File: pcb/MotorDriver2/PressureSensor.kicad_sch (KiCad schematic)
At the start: 22 parts, among them J2 Conn_01x02, J3 Conn_01x02, J4 Conn_01x02, J5 Conn_01x02, U6 LM324DR

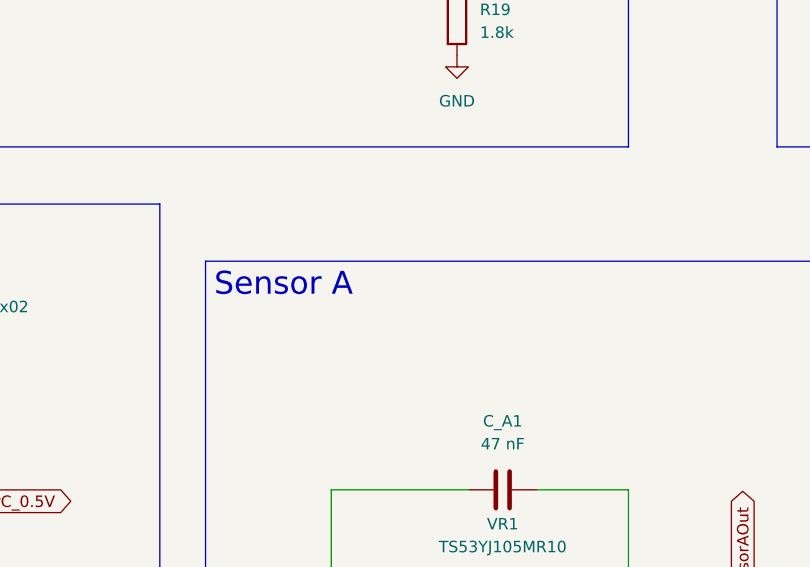
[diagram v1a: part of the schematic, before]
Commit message: Modified pwm pins
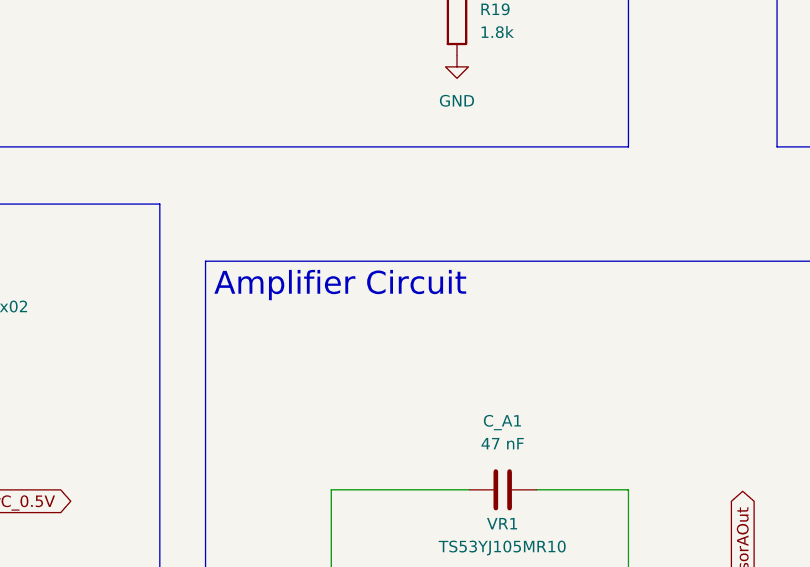
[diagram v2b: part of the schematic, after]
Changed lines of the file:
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@@
 	(generator_version "9.0")
 	(paper "A4")
-	(text_box "Sensor A\n"
+	(text_box "Amplifier Circuit"
 		(exclude_from_sim no)
 		(at 90.17 66.04 0)

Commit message: Laying out PCB
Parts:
- C_A1: LCSC (none) -> C77012
- R18, R19: LCSC (none) -> C25871
- U6: footprint footprintLib:D14 -> CapstoneFootprints:D14
- VR1, VR2, VR3, VR4: footprint footprintLib:TS53YJ105MR10 -> CapstoneFootprints:TS53YJ105MR10
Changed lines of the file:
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@@
 		(dnp no)
 		(fields_autoplaced yes)
-		(property "Reference" "#PWR065"
+		(property "Reference" "#PWR025"
 			(at 60.96 111.76 0)
 			(effects
@@
 			(project "MotorDriver1"
 				(path "/6e0510ec-6dbc-4bc1-a315-3680b1127a92/84d965bc-7f0b-4bc5-931c-8ce848efd12b"
-					(reference "#PWR065")
+					(reference "#PWR025")
 					(unit 1)
 				)
@@
 		(dnp no)
 		(fields_autoplaced yes)
-		(property "Reference" "#PWR042"
+		(property "Reference" "#PWR026"
 			(at 60.96 171.45 0)
 			(effects
@@
 			(project "MotorDriver1"
 				(path "/6e0510ec-6dbc-4bc1-a315-3680b1127a92/84d965bc-7f0b-4bc5-931c-8ce848efd12b"
-					(reference "#PWR042")
+					(reference "#PWR026")
 					(unit 1)
 				)
@@
 			)
 		)
+		(property "LCSC" "C25871"
+			(at 118.11 39.37 0)
+			(effects
+				(font
+					(size 1.27 1.27)
+				)
+				(hide yes)
+			)
+		)
 		(pin "2"
 		)
@@
 		(dnp no)
 		(fields_autoplaced yes)
-		(property "Reference" "#PWR062"
+		(property "Reference" "#PWR029"
 			(at 185.42 40.64 0)
 			(effects
@@
 			(project "MotorDriver1"
 				(path "/6e0510ec-6dbc-4bc1-a315-3680b1127a92/84d965bc-7f0b-4bc5-931c-8ce848efd12b"
-					(reference "#PWR062")
+					(reference "#PWR029")
 					(unit 1)
 				)
@@
 		(dnp no)
 		(fields_autoplaced yes)
-		(property "Reference" "#PWR064"
+		(property "Reference" "#PWR023"
 			(at 52.07 77.47 0)
 			(effects
@@
 			(project "MotorDriver1"
 				(path "/6e0510ec-6dbc-4bc1-a315-3680b1127a92/84d965bc-7f0b-4bc5-931c-8ce848efd12b"
-					(reference "#PWR064")
+					(reference "#PWR023")
 					(unit 1)
 				)
@@
 		(dnp no)
 		(fields_autoplaced yes)
-		(property "Reference" "#PWR041"
+		(property "Reference" "#PWR024"
 			(at 52.07 137.16 0)
 			(effects
@@
 			(project "MotorDriver1"
 				(path "/6e0510ec-6dbc-4bc1-a315-3680b1127a92/84d965bc-7f0b-4bc5-931c-8ce848efd12b"
-					(reference "#PWR041")
+					(reference "#PWR024")
 					(unit 1)
 				)
@@
 		(dnp no)
 		(fields_autoplaced yes)
-		(property "Reference" "#PWR043"
+		(property "Reference" "#PWR028"
 			(at 118.11 49.53 0)
 			(effects
@@
 			(project "MotorDriver1"
 				(path "/6e0510ec-6dbc-4bc1-a315-3680b1127a92/84d965bc-7f0b-4bc5-931c-8ce848efd12b"
-					(reference "#PWR043")
+					(reference "#PWR028")
 					(unit 1)
 				)
@@
 		(dnp no)
 		(fields_autoplaced yes)
-		(property "Reference" "#PWR040"
+		(property "Reference" "#PWR027"
 			(at 62.23 40.64 0)
 			(effects
@@
 			(project "MotorDriver1"
 				(path "/6e0510ec-6dbc-4bc1-a315-3680b1127a92/84d965bc-7f0b-4bc5-931c-8ce848efd12b"
-					(reference "#PWR040")
+					(reference "#PWR027")
 					(unit 1)
 				)
@@
 			)
 		)
-		(property "Footprint" "footprintLib:TS53YJ105MR10"
+		(property "Footprint" "CapstoneFootprints:TS53YJ105MR10"
 			(at 226.06 238.43 0)
 			(effects
@@
 		(dnp no)
 		(fields_autoplaced yes)
-		(property "Reference" "#PWR063"
+		(property "Reference" "#PWR032"
 			(at 241.3 49.53 0)
 			(effects
@@
 			(project "MotorDriver1"
 				(path "/6e0510ec-6dbc-4bc1-a315-3680b1127a92/84d965bc-7f0b-4bc5-931c-8ce848efd12b"
-					(reference "#PWR063")
+					(reference "#PWR032")
 					(unit 1)
 				)
@@
 			)
 		)
-		(property "Footprint" "footprintLib:D14"
+		(property "Footprint" "CapstoneFootprints:D14"
 			(at 162.56 106.68 0)
 			(effects
@@
 			)
 		)
+		(property "LCSC" "C25871"
+			(at 60.96 161.29 0)
+			(effects
+				(font
+					(size 1.27 1.27)
+				)
+				(hide yes)
+			)
+		)
 		(pin "2"
 		)
@@
 			)
 		)
+		(property "LCSC" "C77012"
+			(at 123.19 91.44 0)
+			(effects
+				(font
+					(size 1.27 1.27)
+				)
+				(hide yes)
+			)
+		)
 		(pin "2"
 		)
@@
 		(dnp no)
 		(fields_autoplaced yes)
-		(property "Reference" "#PWR044"
+		(property "Reference" "#PWR031"
 			(at 215.9 114.3 0)
 			(effects
@@
 			(project ""
 				(path "/6e0510ec-6dbc-4bc1-a315-3680b1127a92/84d965bc-7f0b-4bc5-931c-8ce848efd12b"
-					(reference "#PWR044")
+					(reference "#PWR031")
 					(unit 1)
 				)
@@
 		(dnp no)
 		(fields_autoplaced yes)
-		(property "Reference" "#PWR0101"
+		(property "Reference" "#PWR030"
 			(at 203.2 87.63 0)
 			(effects
@@
 			(project "MotorDriver1"
 				(path "/6e0510ec-6dbc-4bc1-a315-3680b1127a92/84d965bc-7f0b-4bc5-931c-8ce848efd12b"
-					(reference "#PWR0101")
+					(reference "#PWR030")
 					(unit 1)
 				)
@@
 			)
 		)
-		(property "Footprint" "footprintLib:TS53YJ105MR10"
+		(property "Footprint" "CapstoneFootprints:TS53YJ105MR10"
 			(at 231.14 197.79 0)
 			(effects
@@
 			)
 		)
-		(property "Footprint" "footprintLib:TS53YJ105MR10"
+		(property "Footprint" "CapstoneFootprints:TS53YJ105MR10"
 			(at 148.59 237.16 0)
 			(effects
@@
 			)
 		)
-		(property "Footprint" "footprintLib:TS53YJ105MR10"
+		(property "Footprint" "CapstoneFootprints:TS53YJ105MR10"
 			(at 133.35 197.79 0)
 			(effects

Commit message: Made some edits while making design poster
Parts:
- added C_A3: 47 pF, Capacitor_SMD:C_0402_1005Metric, symbol Device:C
- added R10: 10k, Resistor_SMD:R_0402_1005Metric, symbol Device:R
- added R20: 1.8k, Resistor_SMD:R_0402_1005Metric, symbol Device:R
- added U4: ADS1015IDGS, Package_SO:TSSOP-10_3x3mm_P0.5mm, symbol Analog_ADC:ADS1015IDGS
- added U5: MCP6L01Rx-xOT, Package_TO_SOT_SMD:SOT-23-5, symbol Amplifier_Operational:MCP6L01Rx-xOT
- added VR5: TS53YJ105MR10, CapstoneFootprints:TS53YJ105MR10, symbol pcb:TS53YJ105MR10
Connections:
- net 3V3: now also R10.1, U4.8 (VDD), U5.2 (V+)
- net GND: now also R20.2, U4.1 (ADDR), U4.3 (GND), U5.5 (V-)
- net SensorAIn: now also C_A3.2, U5.4 (-), VR5.A1 (CCW)
- new net: R10.2, R20.1, U5.3 (+)
- new net SCL: U4.10 (SCL)
- new net SDA: U4.9 (SDA)
- new net SensorAAmp: C_A3.1, U4.4 (AIN0), U5.1, VR5.B1 (WIPER)
- new net SensorBAmp: U4.5 (AIN1)
- new net SensorCAmp: U4.6 (AIN2)
- new net SensorDAmp: U4.7 (AIN3)
- no-connect marks 4 -> 5
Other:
- note added: "0.5 V bias"
- note added: "potentiometer"
